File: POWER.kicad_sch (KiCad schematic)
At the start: 85 parts, among them IC1801 ${DEVICE}, IC1802 ${DEVICE}, IC1803 ${DEVICE}, IC1804 ${DEVICE}, IC3 ${DEVICE}, J1801 ${FAMILY}, J1802 ${FAMILY}, J1803 ${FAMILY}

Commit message: Rerouted PCB Logic part
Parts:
- renumbered C1820 to C9901, C2 to C9902, C1821 to C9903, C1826 to C9904, C3 to C9905, C1822 to C9906, C1827 to C9907, C4 to C9908, C1801 to C9909, C1811 to C9910, C1828 to C9911, C1829 to C9912, C1802 to C9913, C1812 to C9914, C1823 to C9915, C1830 to C9916, C5 to C9917, C1803 to C9918, C1813 to C9919, C1824 to C9920, C6 to C9921, C1825 to C9922, C1810 to C9923, C7 to C9924, C1804 to C9925, C1814 to C9926, C1805 to C9927, C1815 to C9928, C1806 to C9929, C1816 to C9930, C1831 to C9931, C1832 to C9932, C1833 to C9933, C1834 to C9934, C1807 to C9935, C1817 to C9936, C1808 to C9937, C1818 to C9938, C1809 to C9939, C1819 to C9940, IC1803 to IC9901, IC1804 to IC9902, IC3 to IC9903, IC1801 to IC9904, IC1802 to IC9905, J1801 to J9901, J1802 to J9902, J1803 to J9903, L1805 to L9901, L1804 to L9902, L2 to L9903, L1808 to L9904, L1801 to L9905, L1803 to L9906, L1807 to L9907, LD1806 to LD9901, LD1805 to LD9902, LD1 to LD9903, LD1801 to LD9904, LD1803 to LD9905, LD1802 to LD9906, LD1804 to LD9907, R1812 to R9901, R1814 to R9902, R1816 to R9903, R1817 to R9904, R16 to R9905, R17 to R9906, R18 to R9907, R19 to R9908, R1818 to R9909, R1810 to R9910, R20 to R9911, R1801 to R9912, R1807 to R9913, R1803 to R9914, R1804 to R9915, R1805 to R9916, R1806 to R9917, R1809 to R9918, R1811 to R9919, R1813 to R9920, R1815 to R9921, R1802 to R9922, R1808 to R9923

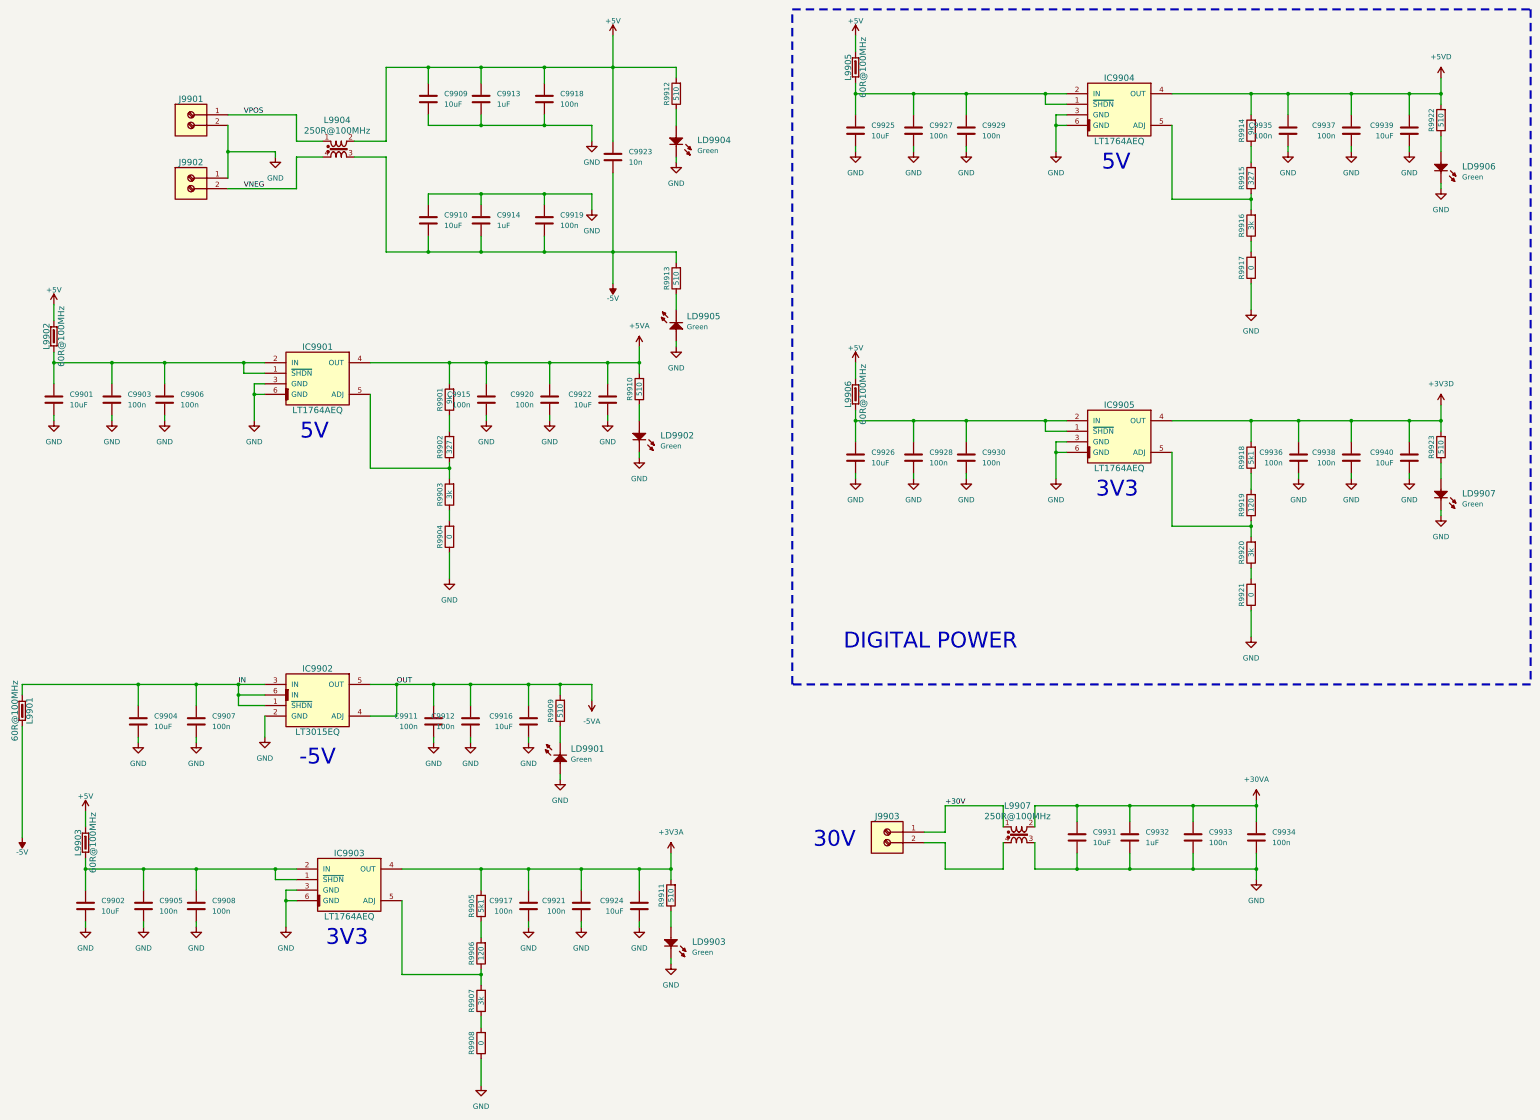
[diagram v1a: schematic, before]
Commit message: Routing the Power Sector
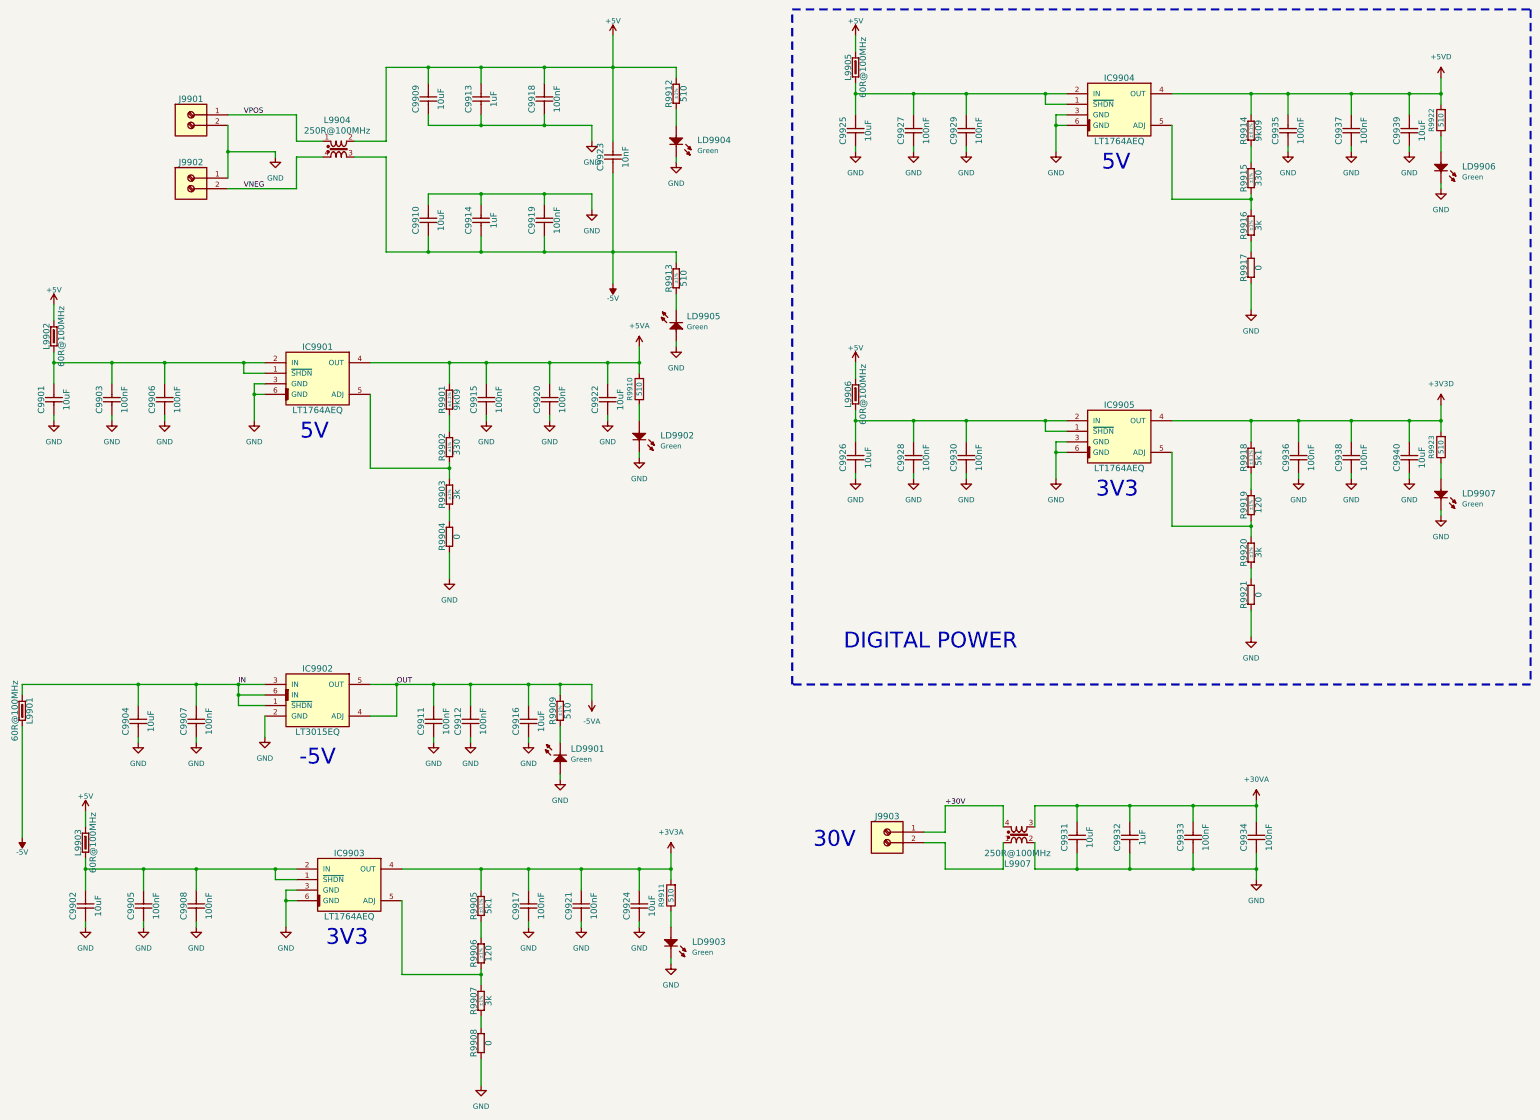
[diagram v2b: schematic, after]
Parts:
- removed C9901, C9902, C9904, C9909, C9910, C9916, C9922, C9924, C9925, C9926, C9931, C9939, C9940: 10uF, Capacitor_SMD:C_1206_3216Metric_Pad1.33x1.80mm_HandSolder, symbol Device:C
- removed C9903, C9905, C9906, C9907, C9908, C9911, C9912, C9915, C9917, C9918, C9919, C9920, C9921, C9927, C9928, C9929, C9930, C9933, C9934, C9935, C9936, C9937, C9938: 100n, Capacitor_SMD:C_0603_1608Metric_Pad1.08x0.95mm_HandSolder, symbol Device:C
- removed C9913, C9914, C9932: 1uF, Capacitor_SMD:C_1206_3216Metric_Pad1.33x1.80mm_HandSolder, symbol Device:C
- removed C9923: 10n, Capacitor_SMD:C_0603_1608Metric_Pad1.08x0.95mm_HandSolder, symbol Device:C
- removed R9901, R9914: 9k, Resistor_SMD:R_0603_1608Metric_Pad0.98x0.95mm_HandSolder, symbol Device:R
- removed R9902, R9915: 327, Resistor_SMD:R_0603_1608Metric_Pad0.98x0.95mm_HandSolder, symbol Device:R
- removed R9903, R9907, R9916, R9920: 3k, Resistor_SMD:R_0603_1608Metric_Pad0.98x0.95mm_HandSolder, symbol Device:R
- removed R9904, R9908, R9917, R9921: 0, Resistor_SMD:R_0603_1608Metric_Pad0.98x0.95mm_HandSolder, symbol Device:R
- removed R9905, R9918: 5k1, Resistor_SMD:R_0603_1608Metric_Pad0.98x0.95mm_HandSolder, symbol Device:R
- removed R9906, R9919: 120, Resistor_SMD:R_0603_1608Metric_Pad0.98x0.95mm_HandSolder, symbol Device:R
- removed R9909, R9912, R9913: 510, Resistor_SMD:R_0603_1608Metric_Pad0.98x0.95mm_HandSolder, symbol Device:R
- added C9901, C9902, C9904, C9909, C9910, C9916, C9922, C9924, C9925, C9926, C9931, C9939, C9940: 10uF, Capacitors SMD:CAPC3216X180N, symbol CERN:Capacitors SMD/CC1206_10UF_50V_10%_X5R
- added C9903, C9905, C9906, C9907, C9908, C9911, C9912, C9915, C9917, C9918, C9919, C9920, C9921, C9927, C9928, C9929, C9930, C9933, C9934, C9935, C9936, C9937, C9938: 100nF, Capacitors SMD:CAPC1608X87N, symbol CERN:Capacitors SMD/CC0603_100NF_50V_10%_X5R
- added C9913, C9914, C9932: 1uF, Capacitors SMD:CAPC3216X180N, symbol CERN:Capacitors SMD/CC1206_1UF_50V_5%_X7R
- added C9923: 10nF, Capacitors SMD:CAPC1608X87N, symbol CERN:Capacitors SMD/CC0603_10NF_50V_5%_C0G
- added R9901, R9914: 9k09, Resistors SMD:RESC1608X55N, symbol CERN:Resistors SMD/R0603_9K09_0.1%_0.063W_10PPM
- added R9902, R9915: 330, Resistors SMD:RESC1608X55N, symbol CERN:Resistors SMD/R0603_330R_1%_0.1W_100PPM
- added R9903, R9907, R9916, R9920: 3k, Resistors SMD:RESC1608X55N, symbol CERN:Resistors SMD/R0603_3K_1%_0.1W_100PPM
- added R9904, R9908, R9917, R9921: 0, Resistors SMD:RESC1608X55N, symbol CERN:Resistors SMD/R0603_0R_JUMPER
- added R9905, R9918: 5k1, Resistors SMD:RESC1608X64N, symbol CERN:Resistors SMD/R0603_5K1_0.1%_0.1W_25PPM
- added R9906, R9919: 120, Resistors SMD:RESC1608X55N, symbol CERN:Resistors SMD/R0603_120R_1%_0.1W_100PPM
- added R9909, R9912, R9913: 510, Resistors SMD:RESC1608X55N, symbol CERN:Resistors SMD/R0603_510R_1%_0.1W_100PPM
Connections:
- net +30V: now also L9907.4; no longer L9907.1
- net +30VA: now also L9907.3, C9931.2, C9932.2, C9933.2, C9934.2; no longer L9907.2
- net +3V3A: now also C9917.2, C9921.2, C9924.2, R9905.2
- net +3V3D: now also C9936.2, C9938.2, C9940.2, R9918.2
- net +5V: now also C9909.2, C9913.2, C9918.2, C9923.2, R9912.2
- net +5VA: now also C9915.2, C9920.2, C9922.2, R9901.2
- net +5VD: now also C9935.2, C9937.2, C9939.2, R9914.2
- net -5V: now also C9910.1, C9914.1, C9919.1, C9923.1, R9913.2
- net -5VA: now also C9911.2, C9912.2, C9916.2, R9909.2
- net GND: now also L9907.2, C9901.1, C9902.1, C9903.1, C9904.1, C9905.1, C9906.1, C9907.1, C9908.1, C9909.1, C9910.2, C9911.1, C9912.1, C9913.1, C9914.2, C9915.1, C9916.1, C9917.1, C9918.1, C9919.2, C9920.1, C9921.1, C9922.1, C9924.1, C9925.1, C9926.1, C9927.1, C9928.1, C9929.1, C9930.1, C9931.1, C9932.1, C9933.1, C9934.1, C9935.1, C9936.1, C9937.1, C9938.1, C9939.1, C9940.1, R9904.1, R9908.1, R9917.1, R9921.1; no longer L9907.3
- net IN: now also C9904.2, C9907.2
- net at IC9905.5 (ADJ): now also R9919.1, R9920.2
- net at IC9904.1 (~{SHDN}), IC9904.2 (IN), L9905.1: now also C9925.2, C9927.2, C9929.2
- net at IC9903.5 (ADJ): now also R9906.1, R9907.2
- net at IC9901.1 (~{SHDN}), IC9901.2 (IN), L9902.1: now also C9901.2, C9903.2, C9906.2
- net at IC9903.1 (~{SHDN}), IC9903.2 (IN), L9903.1: now also C9902.2, C9905.2, C9908.2
- net at LD9904.2 (A): now also R9912.1
- net at LD9901.1 (C): now also R9909.1
- net at J9903.2: now also L9907.1; no longer L9907.4
- net at IC9901.5 (ADJ): now also R9902.1, R9903.2
- net at LD9905.1 (C): now also R9913.1
- net at IC9905.1 (~{SHDN}), IC9905.2 (IN), L9906.1: now also C9926.2, C9928.2, C9930.2
- net at IC9904.5 (ADJ): now also R9915.1, R9916.2
- new net: R9901.1, R9902.2
- new net: R9916.1, R9917.2
- new net: R9905.1, R9906.2
- new net: R9907.1, R9908.2
- new net: R9903.1, R9904.2
- new net: R9920.1, R9921.2
- new net: R9914.1, R9915.2
- new net: R9918.1, R9919.2

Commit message: Inverted the VGA output
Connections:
- net IN_3V3_D: now reaches C9926.2, C9928.2, C9930.2, IC9905.1 (~{SHDN}), IC9905.2 (IN), L9906.1
- net IN_3V3_A: now reaches C9902.2, C9905.2, C9908.2, IC9903.1 (~{SHDN}), IC9903.2 (IN), L9903.1
- net IN_5VA: now reaches C9901.2, C9903.2, C9906.2, IC9901.1 (~{SHDN}), IC9901.2 (IN), L9902.1
- net IN_5V_D: now reaches C9925.2, C9927.2, C9929.2, IC9904.1 (~{SHDN}), IC9904.2 (IN), L9905.1
- net IN renamed IN_NEG_5V
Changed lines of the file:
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@@
+		)
+	)
+	(label "IN_5V_D"
+		(at 232.41 35.56 0)
+		(effects
+			(font
+				(size 1.27 1.27)
+			)
+			(justify left bottom)
 		)
 	)
@@
 		)
 	)
+	(label "IN_NEG_5V"
+		(at 45.72 177.8 0)
+		(effects
+			(font
+				(size 1.27 1.27)
+			)
+			(justify left bottom)
+		)
+	)
+	(label "IN_5VA"
+		(at 39.37 100.33 0)
+		(effects
+			(font
+				(size 1.27 1.27)
+			)
+			(justify left bottom)
+		)
+	)
 	(label "VNEG"
 		(at 71.12 58.42 0)
@@
 		)
 	)
-	(label "IN"
-		(at 69.85 177.8 0)
+	(label "IN_3V3_A"
+		(at 46.99 222.25 0)
+		(effects
+			(font
+				(size 1.27 1.27)
+			)
+			(justify left bottom)
+		)
+	)
+	(label "IN_3V3_D"
+		(at 232.41 114.3 0)
 		(effects
 			(font
@@
 		)
 	)
+	(rule_area
+		(polyline
+			(pts
+				(xy 213.36 16.51) (xy 213.36 58.42) (xy 219.71 64.77) (xy 307.34 64.77) (xy 307.34 93.98) (xy 308.61 95.25)
+				(xy 317.5 95.25) (xy 320.04 92.71) (xy 320.04 59.69) (xy 322.58 57.15) (xy 355.6 57.15) (xy 356.87 58.42)
+				(xy 356.87 64.77) (xy 358.14 66.04) (xy 363.22 66.04) (xy 364.49 64.77) (xy 364.49 30.48) (xy 361.95 27.94)
+				(xy 358.14 27.94) (xy 353.06 33.02) (xy 295.91 33.02) (xy 276.86 13.97) (xy 215.9 13.97)
+			)
+			(stroke
+				(width 0)
+				(type dash)
+			)
+			(fill
+				(type none)
+			)
+		)
+	)
+	(rule_area
+		(polyline
+			(pts
+				(xy 20.32 81.28) (xy 20.32 123.19) (xy 26.67 129.54) (xy 114.3 129.54) (xy 114.3 158.75) (xy 115.57 160.02)
+				(xy 124.46 160.02) (xy 127 157.48) (xy 127 124.46) (xy 129.54 121.92) (xy 162.56 121.92) (xy 163.83 123.19)
+				(xy 163.83 129.54) (xy 165.1 130.81) (xy 170.18 130.81) (xy 171.45 129.54) (xy 171.45 95.25) (xy 168.91 92.71)
+				(xy 165.1 92.71) (xy 160.02 97.79) (xy 102.87 97.79) (xy 83.82 78.74) (xy 22.86 78.74)
+			)
+			(stroke
+				(width 0)
+				(type dash)
+			)
+			(fill
+				(type none)
+			)
+		)
+	)
+	(rule_area
+		(polyline
+			(pts
+				(xy 213.36 93.98) (xy 213.36 135.89) (xy 219.71 142.24) (xy 307.34 142.24) (xy 307.34 171.45) (xy 308.61 172.72)
+				(xy 317.5 172.72) (xy 320.04 170.18) (xy 320.04 137.16) (xy 322.58 134.62) (xy 355.6 134.62) (xy 356.87 135.89)
+				(xy 356.87 142.24) (xy 358.14 143.51) (xy 363.22 143.51) (xy 364.49 142.24) (xy 364.49 107.95) (xy 361.95 105.41)
+				(xy 358.14 105.41) (xy 353.06 110.49) (xy 295.91 110.49) (xy 276.86 91.44) (xy 215.9 91.44)
+			)
+			(stroke
+				(width 0)
+				(type dash)
+			)
+			(fill
+				(type none)
+			)
+		)
+	)
+	(rule_area
+		(polyline
+			(pts
+				(xy 27.94 201.93) (xy 27.94 243.84) (xy 34.29 250.19) (xy 121.92 250.19) (xy 121.92 279.4) (xy 123.19 280.67)
+				(xy 132.08 280.67) (xy 134.62 278.13) (xy 134.62 245.11) (xy 137.16 242.57) (xy 170.18 242.57) (xy 171.45 243.84)
+				(xy 171.45 250.19) (xy 172.72 251.46) (xy 177.8 251.46) (xy 179.07 250.19) (xy 179.07 215.9) (xy 176.53 213.36)
+				(xy 172.72 213.36) (xy 167.64 218.44) (xy 110.49 218.44) (xy 91.44 199.39) (xy 30.48 199.39)
+			)
+			(stroke
+				(width 0)
+				(type dash)
+			)
+			(fill
+				(type none)
+			)
+		)
+	)
+	(netclass_flag ""
+		(length 2.54)
+		(shape round)
+		(at 22.86 78.74 0)
+		(fields_autoplaced yes)
+		(effects
+			(font
+				(size 1.27 1.27)
+			)
+			(justify left bottom)
+		)
+		(property "Netclass" ""
+			(at -138.43 11.43 0)
+			(effects
+				(font
+					(size 1.27 1.27)
+				)
+			)
+		)
+		(property "Component Class" "LDO1"
+			(at 23.5585 76.2 0)
+			(effects
+				(font
+					(size 1.27 1.27)
+					(italic yes)
+				)
+				(justify left)
+			)
+		)
+	)
+	(netclass_flag ""
+		(length 2.54)
+		(shape round)
+		(at 30.48 199.39 0)
+		(fields_autoplaced yes)
+		(effects
+			(font
+				(size 1.27 1.27)
+			)
+			(justify left bottom)
+		)
+		(property "Netclass" ""
+			(at -130.81 132.08 0)
+			(effects
+				(font
+					(size 1.27 1.27)
+				)
+			)
+		)
+		(property "Component Class" "LDO2"
+			(at 31.1785 196.85 0)
+			(effects
+				(font
+					(size 1.27 1.27)
+					(italic yes)
+				)
+				(justify left)
+			)
+		)
+	)
+	(netclass_flag ""
+		(length 2.54)
+		(shape round)
+		(at 215.9 13.97 0)
+		(fields_autoplaced yes)
+		(effects
+			(font
+				(size 1.27 1.27)
+			)
+			(justify left bottom)
+		)
+		(property "Netclass" ""
+			(at 54.61 -53.34 0)
+			(effects
+				(font
+					(size 1.27 1.27)
+				)
+			)
+		)
+		(property "Component Class" "LDO4"
+			(at 216.5985 11.43 0)
+			(effects
+				(font
+					(size 1.27 1.27)
+					(italic yes)
+				)
+				(justify left)
+			)
+		)
+	)
+	(netclass_flag ""
+		(length 2.54)
+		(shape round)
+		(at 215.9 91.44 0)
+		(fields_autoplaced yes)
+		(effects
+			(font
+				(size 1.27 1.27)
+			)
+			(justify left bottom)
+		)
+		(property "Netclass" ""
+			(at 54.61 24.13 0)
+			(effects
+				(font
+					(size 1.27 1.27)
+				)
+			)
+		)
+		(property "Component Class" "LDO3"
+			(at 216.5985 88.9 0)
+			(effects
+				(font
+					(size 1.27 1.27)
+					(italic yes)
+				)
+				(justify left)
+			)
+		)
+	)
